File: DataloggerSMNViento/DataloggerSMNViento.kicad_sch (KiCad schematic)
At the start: 0 parts

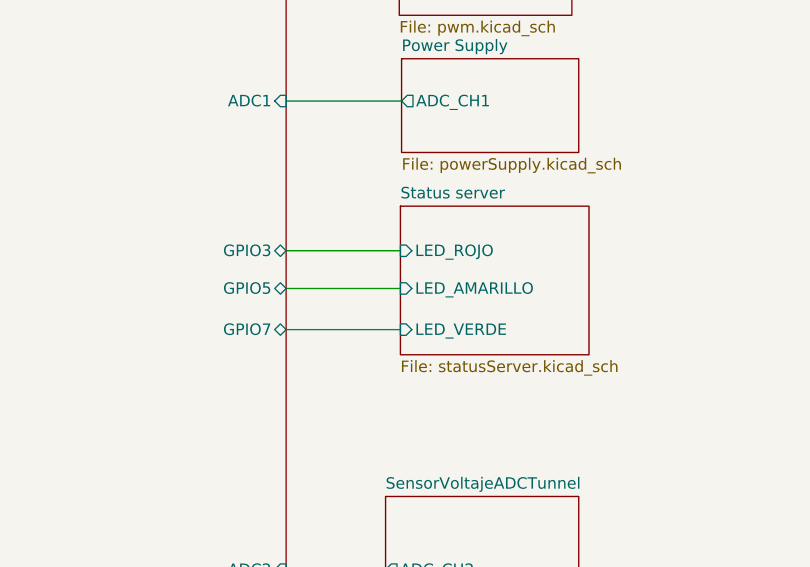
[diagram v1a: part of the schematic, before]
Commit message: Subo la version v1.2 THT de la poncho, para fabricar en el SMN
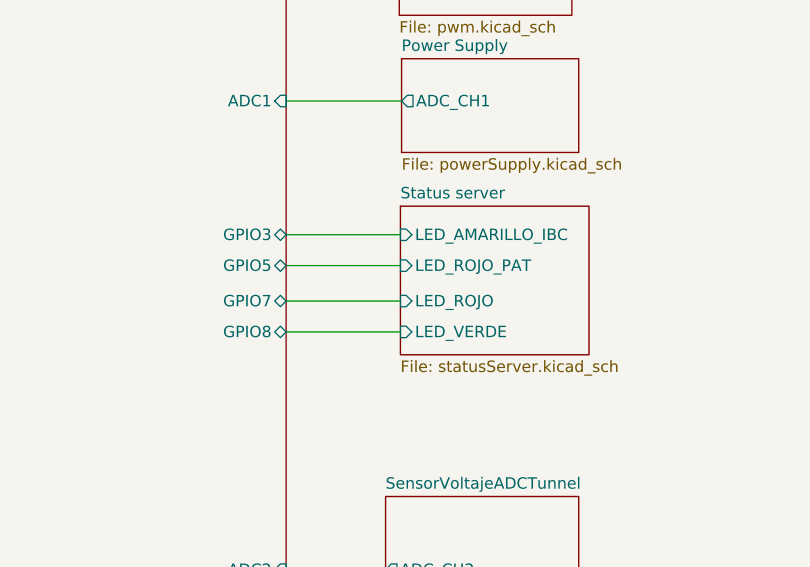
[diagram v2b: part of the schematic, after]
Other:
- sheet Conector del Poncho ports: added GPIO8; removed none
- sheet Status server ports: added LED_AMARILLO_IBC, LED_ROJO_PAT; removed LED_AMARILLO
